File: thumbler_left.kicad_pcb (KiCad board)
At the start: 4 copper layers, 188 x 209 mm, 257 parts, among them J1 USB_B_Micro, J2 Conn_01x04, J3 Conn_01x04, J4 DIN-5_180degree, J5 Conn_01x04, J6 DIN-5_180degree, J7 Conn_01x04, J8 USB_B_Micro, J9 Conn_02x04_Top_Bottom, SW1 SW_Push, SW2 SW_DIP_x05, SW3 SW_Push, SW4 SW_DIP_x05, U1 STM32F072C8Tx, U2 MCP1700-3302E_SOT89, U3 MCP1700-3302E_SOT89, U4 STM32F072C8Tx

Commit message: staritng to split files
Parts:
- removed C11, C12: Cext, Capacitor_SMD:C_0805_2012Metric_Pad1.18x1.45mm_HandSolder
- removed C13: 100n, Capacitor_SMD:C_0805_2012Metric_Pad1.18x1.45mm_HandSolder
- removed C14, C15: 1u, Capacitor_SMD:C_0805_2012Metric_Pad1.18x1.45mm_HandSolder
- removed C16, C17: 4u7, Capacitor_SMD:C_0603_1608Metric_Pad1.08x0.95mm_HandSolder
- removed C18, C19, C20: 100n, Capacitor_SMD:C_0603_1608Metric_Pad1.08x0.95mm_HandSolder
- removed C21: 1u, Capacitor_SMD:C_0603_1608Metric_Pad1.08x0.95mm_HandSolder
- removed C22: 10n, Capacitor_SMD:C_0603_1608Metric_Pad1.08x0.95mm_HandSolder
- removed D36, D37, D38, D39, D40, D41, D42, D43, D44, D46, D47, D48, D49, D50, D52, D53, D54, D56, D57, D58, D59, D60, D61, D62, D63, D64, D65, D67, D68, D69, D70, D71, D72, D73, D74, D75, D76: 1N4148, Diode_THT:D_DO-35_SOD27_P7.62mm_Horizontal
- removed D45, D51, D55: WHITE, LED_SMD:LED_1206_3216Metric_Pad1.42x1.75mm_HandSolder
- removed D66: B5819W, Diode_SMD:D_SOD-123
- removed D77: RED, LED_SMD:LED_1206_3216Metric_Pad1.42x1.75mm_HandSolder
- removed F2: 350mA, Resistor_SMD:R_1812_4532Metric_Pad1.30x3.40mm_HandSolder
- removed FB2: 90R @ 100MHz, Inductor_SMD:L_0805_2012Metric_Pad1.15x1.40mm_HandSolder
- removed J5, J7: Conn_01x04, Connector_PinHeader_2.54mm:PinHeader_2x02_P2.54mm_Vertical
- removed J6: DIN-5_180degree, Connector_DIN:DIN5_180_CP-2350
- removed J8: USB_B_Micro, Connector_USB:USB_Micro-B_HRO_U-F-M5SS-W-1
- removed R13, R15, R16, R19, R20, R24, R25, R26: 470R, Resistor_SMD:R_0805_2012Metric_Pad1.20x1.40mm_HandSolder
- removed R14, R17, R18, R27: 1K, Resistor_SMD:R_0805_2012Metric_Pad1.20x1.40mm_HandSolder
- removed R21, R22: 22R, Resistor_SMD:R_0805_2012Metric_Pad1.20x1.40mm_HandSolder
- removed R23: 10K, Resistor_SMD:R_0805_2012Metric_Pad1.20x1.40mm_HandSolder
- removed S34: RKJXV122400R, Alps:RKJXV122400R
- removed S35, S36, S37, S38, S39, S40, S41, S42, S43, S44, S45, S46, S47, S48, S49, S50, S51, S52, S53, S54, S55, S56, S57, S58, S59, S60, S61, S62, S63, S64, S65, S66, S67, S68, S69, S70, S71: Kailh_Hotplug, keyswitches:Kailh_socket_MX_platemount
- removed SW3: SW_Push, Button_Switch_THT:SW_PUSH-12mm
- removed SW4: SW_DIP_x05, Button_Switch_THT:SW_DIP_SPSTx05_Slide_9.78x14.88mm_W7.62mm_P2.54mm
- removed TP22, TP23, TP24, TP25, TP26, TP27, TP28, TP29, TP30, TP31, TP32, TP33, TP34, TP35, TP36, TP37, TP38: TestPoint, TestPoint:TestPoint_Pad_D2.0mm
- removed U3: MCP1700-3302E_SOT89, Package_TO_SOT_SMD:SOT-89-3
- removed U4: STM32F072C8Tx, Package_QFP:LQFP-48_7x7mm_P0.5mm
- added REF**: MountingHole_3.2mm_M3, MountingHole:MountingHole_3.2mm_M3, F.Cu at (264.2, 311.8)
- added REF**: MountingHole_3.2mm_M3, MountingHole:MountingHole_3.2mm_M3, F.Cu at (165.1, 256.5)
- added REF**: MountingHole_3.2mm_M3, MountingHole:MountingHole_3.2mm_M3, F.Cu at (87.0, 311.8)
- added REF**: MountingHole_3.2mm_M3, MountingHole:MountingHole_3.2mm_M3, F.Cu at (87.0, 174.0)
- added REF**: MountingHole_3.2mm_M3, MountingHole:MountingHole_3.2mm_M3, F.Cu at (231.8, 174.0)
- moved TP18 3.81 mm to (188.6, 298.4)
- moved TP17 1.91 mm to (188.6, 288.9)
- moved TP20 1.91 mm to (188.6, 295.3)
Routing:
- net +3V3: track 50.2 -> 22.4 mm, vias 10 -> 6
- net R_PTR_Y: track 25.7 -> 0.00 mm
- net +5V: track 145.3 -> 124.4 mm, vias 2 -> 1
- net R_PTR_X: track 16.8 -> 0.00 mm
- net R_PTR_Z: track 10.8 -> 0.00 mm
- net Net-(C14-Pad1): track 9.55 -> 0.00 mm
- net Net-(F2-Pad1): track 5.95 -> 0.00 mm, vias 1 -> 0
- net Net-(J8-Pad3): track 5.38 -> 0.00 mm
- net Net-(J8-Pad2): track 5.35 -> 0.00 mm
- net Net-(D5-Pad2): track 0.00 -> 3.86 mm
- net Net-(D4-Pad2): track 0.00 -> 3.78 mm
- net ~{RST}: track 97.5 -> 93.8 mm
- net Net-(D52-Pad2): track 3.63 -> 0.00 mm
- net Net-(D70-Pad2): track 3.58 -> 0.00 mm
- net Net-(D63-Pad2): track 3.58 -> 0.00 mm
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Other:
- board size 188 x 209 mm -> 187.8 x 180.5 mm
- board text added: "JLCJLCJLCJLC"

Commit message: silkscreen
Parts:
- moved SW1 10.1 mm to (126.5, 151.7), turned to 0 degrees
- moved C4 7.80 mm to (137.8, 139.7)
- moved R7 3.18 mm to (156.8, 144.1)
- moved TP15 0.64 mm to (188.6, 291.5)
- moved TP17 0.63 mm to (188.6, 288.3)
- moved TP18 0.63 mm to (188.6, 297.8)
- moved TP20 0.63 mm to (188.6, 294.6)
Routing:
- net ~{RST}: track 93.8 -> 90.0 mm
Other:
- board text added: "3V3"
- board text added: "5V"
- board text added: "A"
- board text added: "B"
- board text added: "BN"
- board text added: "CLK"
- board text added: "COL1"
- board text added: "COL2"
- board text added: "COL3"
- board text added: "COL4"
- board text added: "COL5"
- board text added: "COL6"
- board text added: "COL7"
- board text added: "COL8"
- board text added: "DFU"
- board text added: "DISABLE"
- board text added: "DN"
- board text added: "ENABLE"
- board text added: "Electronics - and - Electronics Accessories"
- board text added: "GND"
- board text added: "IO"
- board text added: "LF"
- board text added: "Left Hand Rev A"
- board text added: "OPT1"
- board text added: "OPT2"
- board text added: "OPT3"
- board text added: "OPT4"
- board text added: "PWR OK"
- board text added: "RESET"
- board text added: "ROW1"
- board text added: "ROW2"
- board text added: "ROW3"
- board text added: "ROW4"
- board text added: "ROW5"
- board text added: "RST"
- board text added: "RST LINK"
- board text added: "RT"
- board text added: "RX"
- board text added: "Strickland"
- board text added: "TX"
- board text added: "Thumbler Keyboard"
- board text added: "UP"

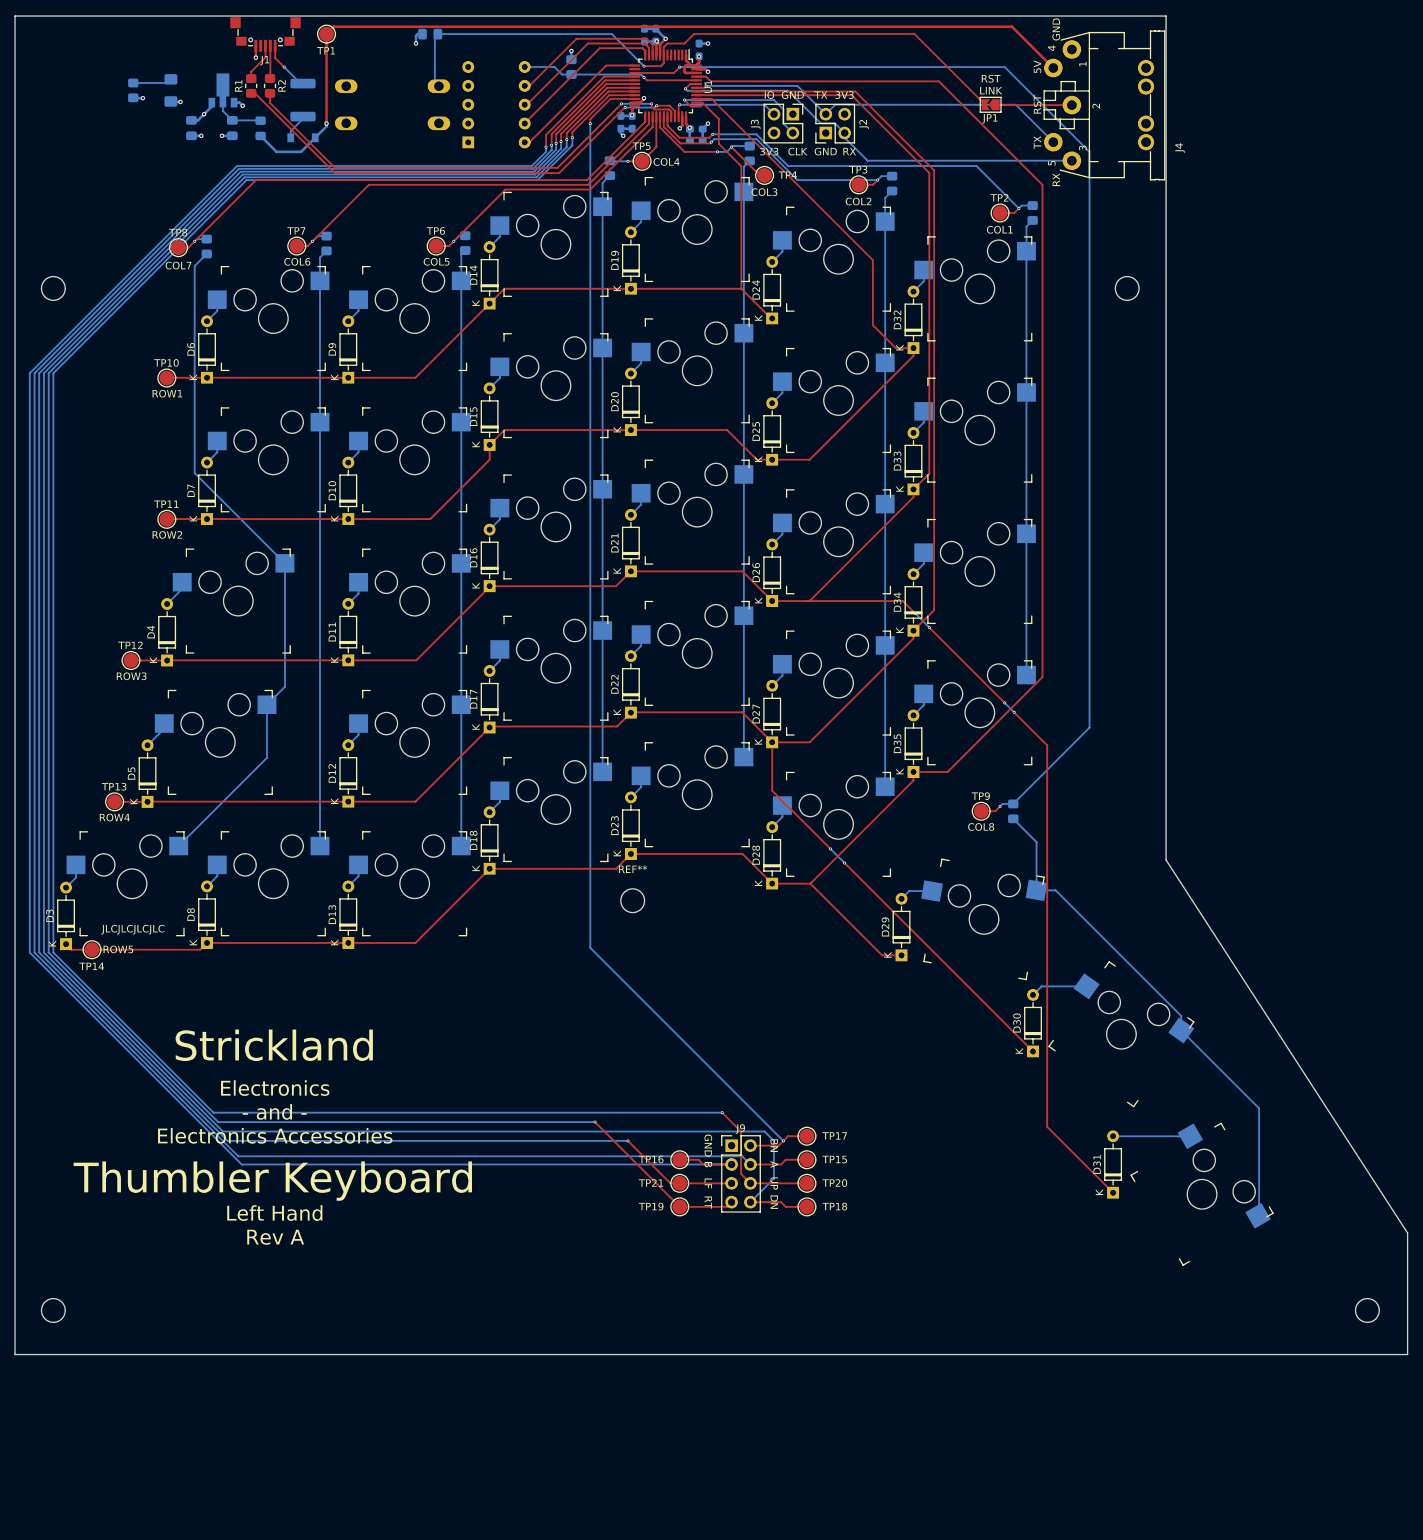
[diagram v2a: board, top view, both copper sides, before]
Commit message: tweak mounting holes
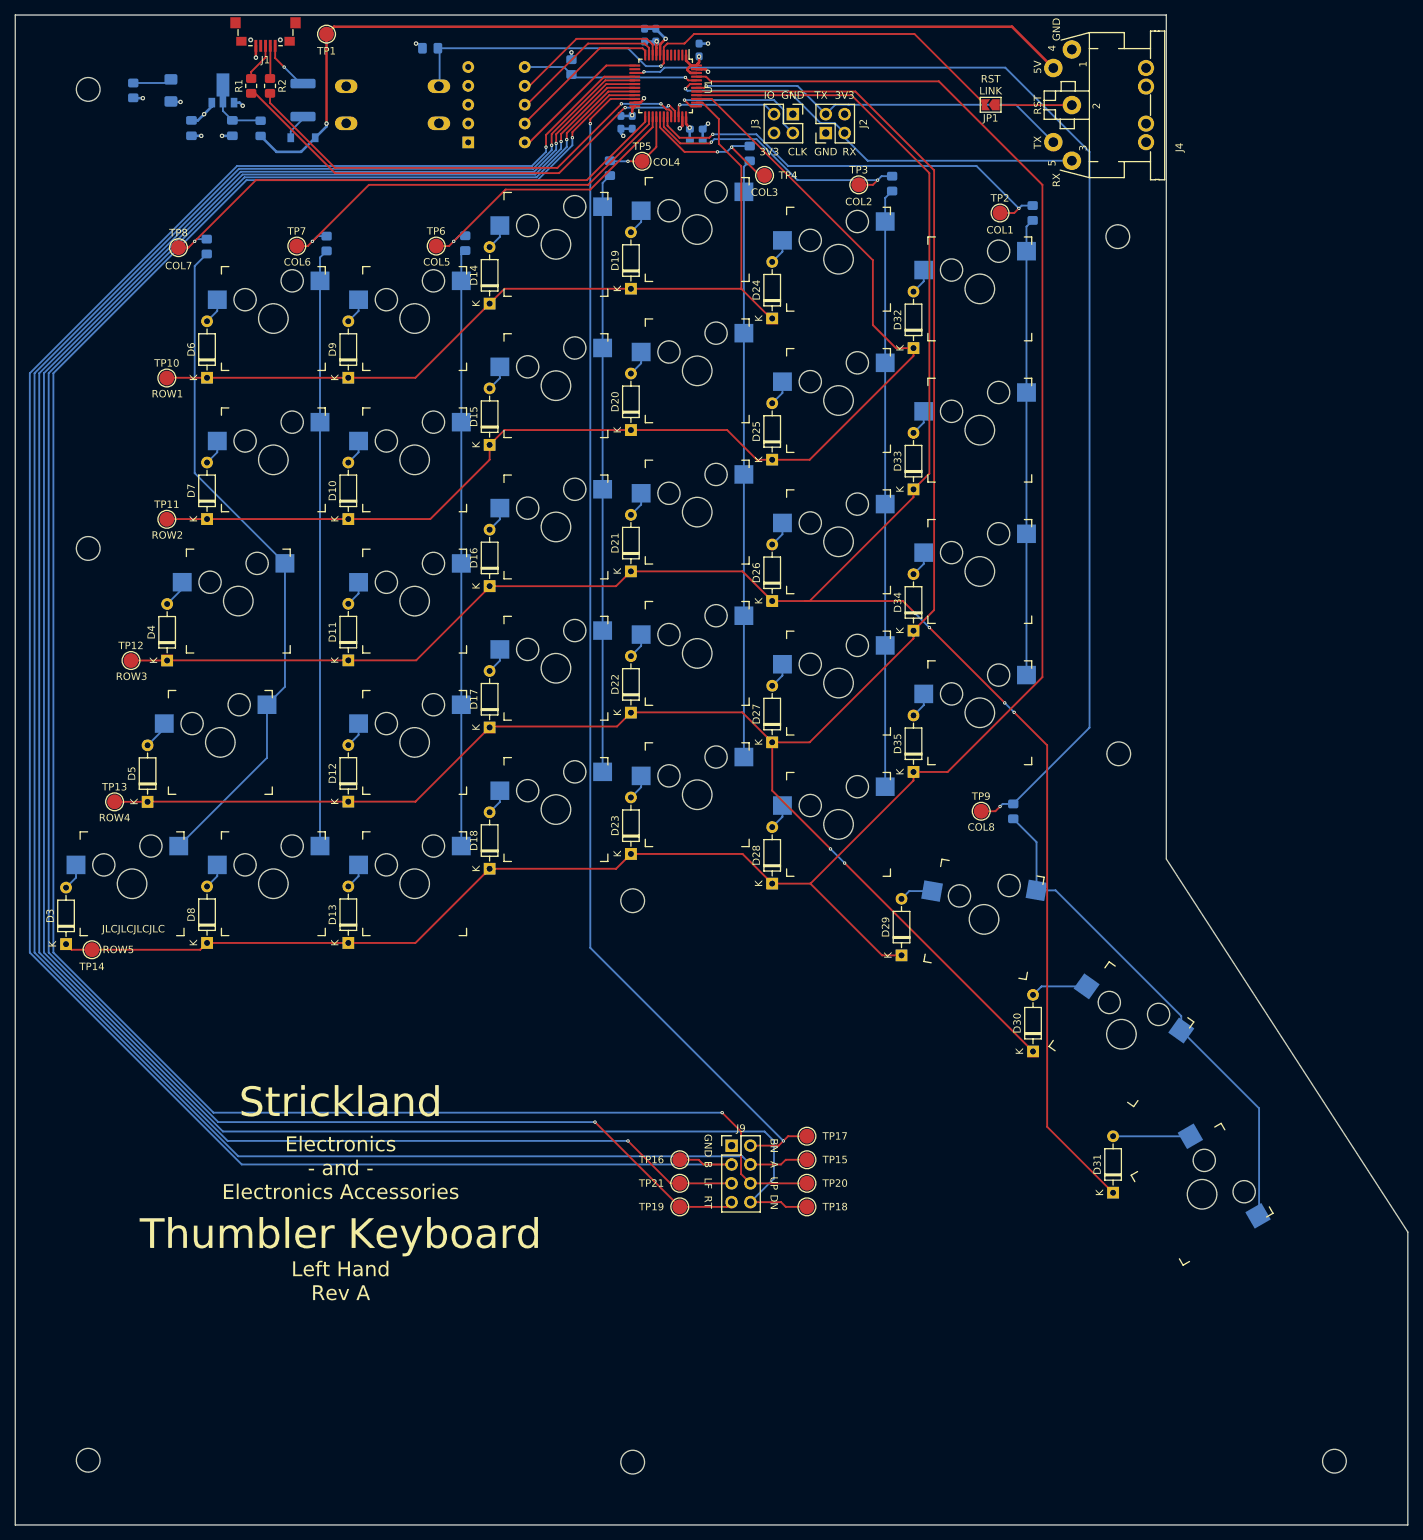
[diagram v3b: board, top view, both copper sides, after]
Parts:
- added REF**: MountingHole_3.2mm_M3, MountingHole:MountingHole_3.2mm_M3, F.Cu at (165.1, 332.2)
- added REF**: MountingHole_3.2mm_M3, MountingHole:MountingHole_3.2mm_M3, F.Cu at (230.6, 236.7)
- added REF**: MountingHole_3.2mm_M3, MountingHole:MountingHole_3.2mm_M3, F.Cu at (91.7, 209.0)
- moved REF** 27.2 mm to (91.7, 147.2)
- moved REF** 20.8 mm to (259.7, 332.1)
- moved REF** 20.7 mm to (91.7, 332.0)
- moved REF** 7.10 mm to (230.5, 167.0)
- moved C4 1.91 mm to (137.8, 141.6)
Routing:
- net ~{RST}: track 90.0 -> 87.1 mm
- net +3V3: track 22.4 -> 21.3 mm
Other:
- board size 187.8 x 180.5 mm -> 187.8 x 203.6 mm
